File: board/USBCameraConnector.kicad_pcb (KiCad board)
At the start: 2 copper layers, 6 parts, among them J1 USB4105-GF-A, J7 Conn_01x04_Pin

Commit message: Done
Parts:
- added REF**: tuna_front_copper_3mm, tuna:tuna_front_copper_3mm, B.Cu at (135.1, 80.0)
- J7: footprint Connector_PinHeader_2.54mm:PinHeader_1x04_P2.54mm_Vertical -> Connector_PinHeader_2.00mm:PinHeader_1x04_P2.00mm_Vertical
- moved J7 6.39 mm to (141.0, 76.8)
- moved R1 4.58 mm to (138.2, 75.7)
- moved R3 4.58 mm to (138.2, 83.3)
- moved R4 4.58 mm to (138.2, 84.3)
- moved R2 4.57 mm to (138.2, 76.7)
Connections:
- J7 pad 2: DP -> DN
- J7 pad 3: DN -> DP
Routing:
- net DP: track 15.9 -> 8.27 mm
- net VBUS: track 0.00 -> 6.79 mm, vias 0 -> 4
- net DN: track 4.76 -> 8.00 mm
- net GND: vias 0 -> 10
- added copper zone on B.Cu, net GND
- added copper zone on F.Cu, net GND
- added copper zone on B.Cu, net Net-(J7-Pin_1)
- added copper zone on F.Cu, net Net-(J7-Pin_1)
- added copper zone on B.Cu, net Net-(J7-Pin_4)
- added copper zone on F.Cu, net Net-(J7-Pin_4)
- added copper zone on B.Cu, net VBUS
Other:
- board outline added: 11.8 x 10.2 mm
- board text added: "*"
- board text added: "5V*: R2&R4 GND*: R1&R3"

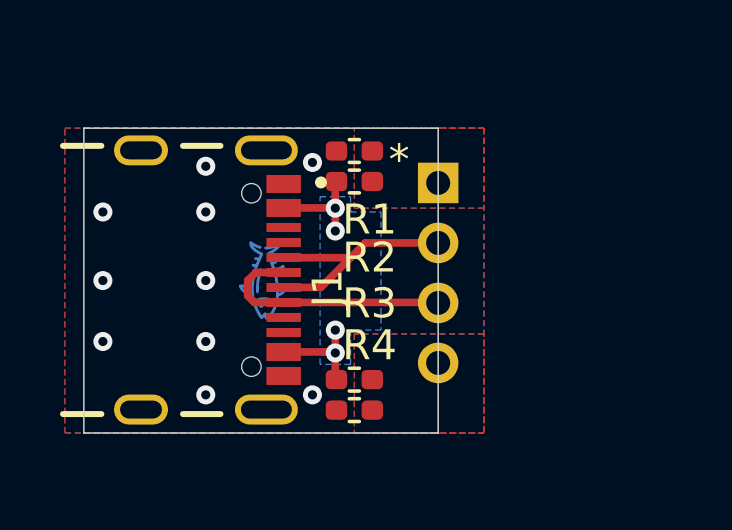
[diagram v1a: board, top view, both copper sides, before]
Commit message: Add github workflow
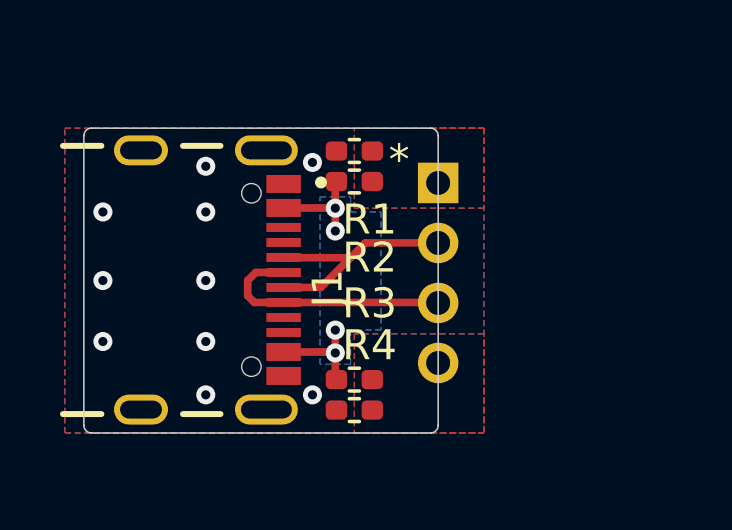
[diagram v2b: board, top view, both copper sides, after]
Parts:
- removed the REF** at (135.1, 80.0)
- added REF**: tuna_soldermask_remove_3mm, tuna:tuna_soldermask_remove_3mm, B.Cu at (135.1, 79.9)
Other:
- outline, holes or cut-outs redrawn

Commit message: Make not castellated holes
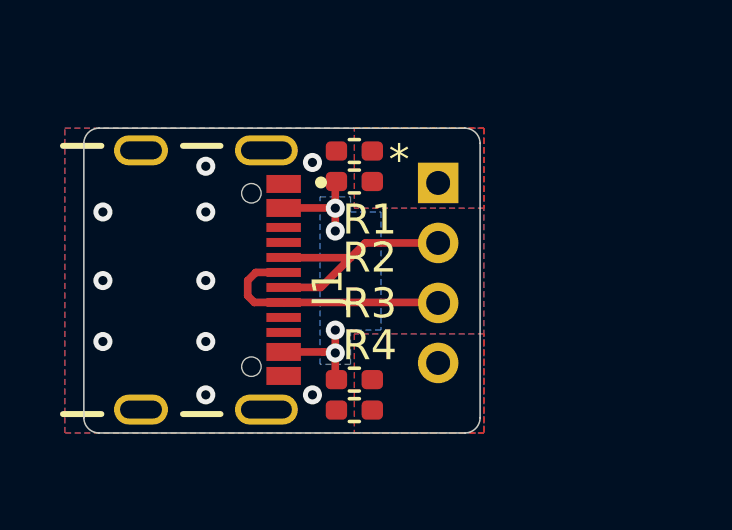
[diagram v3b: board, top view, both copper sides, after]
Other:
- board size 11.8 x 10.2 mm -> 13.2 x 10.2 mm
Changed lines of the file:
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@@
 		(embedded_fonts no)
 	)
-	(gr_line
-		(start 129.413 74.93)
-		(end 140.716 74.93)
+	(gr_arc
+		(start 141.859 74.93)
+		(mid 142.21821 75.07879)
+		(end 142.367 75.438)
+		(stroke
+			(width 0.05)
+			(type default)
+		)
+		(layer "Edge.Cuts")
+	)
+	(gr_arc
+		(start 142.367 84.582)
+		(mid 142.21821 84.94121)
+		(end 141.859 85.09)
+		(stroke
+			(width 0.05)
+			(type default)
+		)
+		(layer "Edge.Cuts")
+	)
+	(gr_arc
+		(start 129.667 85.09)
+		(mid 129.30779 84.94121)
+		(end 129.159 84.582)
 		(stroke
 			(width 0.05)
@@
 	)
 	(gr_line
-		(start 140.97 75.184)
-		(end 140.97 84.836)
+		(start 129.159 84.582)
+		(end 129.159 75.438)
+		(stroke
+			(width 0.05)
+			(type default)
+		)
+		(layer "Edge.Cuts")
+	)
+	(gr_line
+		(start 142.367 75.438)
+		(end 142.367 84.582)
+		(stroke
+			(width 0.05)
+			(type default)
+		)
+		(layer "Edge.Cuts")
+	)
+	(gr_line
+		(start 141.859 85.09)
+		(end 129.667 85.09)
 		(stroke
 			(width 0.05)
@@
 	)
 	(gr_arc
-		(start 129.159 75.184)
-		(mid 129.233395 75.004395)
-		(end 129.413 74.93)
+		(start 129.159 75.438)
+		(mid 129.30779 75.07879)
+		(end 129.667 74.93)
 		(stroke
 			(width 0.05)
@@
 	)
 	(gr_line
-		(start 140.716 85.09)
-		(end 129.413 85.09)
+		(start 129.667 74.93)
+		(end 141.859 74.93)
 		(stroke
 			(width 0.05)
-			(type default)
-		)
-		(layer "Edge.Cuts")
-	)
-	(gr_arc
-		(start 140.97 84.836)
-		(mid 140.895605 85.015605)
-		(end 140.716 85.09)
-		(stroke
-			(width 0.05)
-			(type default)
-		)
-		(layer "Edge.Cuts")
-	)
-	(gr_arc
-		(start 129.413 85.09)
-		(mid 129.233395 85.015605)
-		(end 129.159 84.836)
-		(stroke
-			(width 0.05)
-			(type default)
-		)
-		(layer "Edge.Cuts")
-	)
-	(gr_arc
-		(start 140.716 74.93)
-		(mid 140.895605 75.004395)
-		(end 140.97 75.184)
-		(stroke
-			(width 0.05)
-			(type default)
-		)
-		(layer "Edge.Cuts")
-	)
-	(gr_line
-		(start 129.159 84.836)
-		(end 129.159 75.184)
-		(stroke
-			(width 0.05)
